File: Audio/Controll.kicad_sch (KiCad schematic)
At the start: 44 parts, among them J12 AMP1_PWR, J13 ROTARY_SW, J14 AMP_PWR_IN, J15 PD_IN, J16 AUDIO_IN, J17 OLED_PIN, J18 AMP1_LR, J19 AMP2_PWR, J20 AMP2_LR, J21 AMP3_PWR, J22 AMP4_PWR, J23 AMP5_PWR, J24 AMP3_LR, J25 AMP4_LR, J26 AMP5_LR, K1 AZ850P2-x, K10 AZ850P2-x, K2 AZ850P2-x, K3 AZ850P2-x, K4 AZ850P2-x, K5 AZ850P2-x, K6 AZ850P2-x, K7 AZ850P2-x, K8 AZ850P2-x, K9 AZ850P2-x, U5 BP5293-50, U6 ULN2803A, U7 ULN2803A, U8 ULN2803A

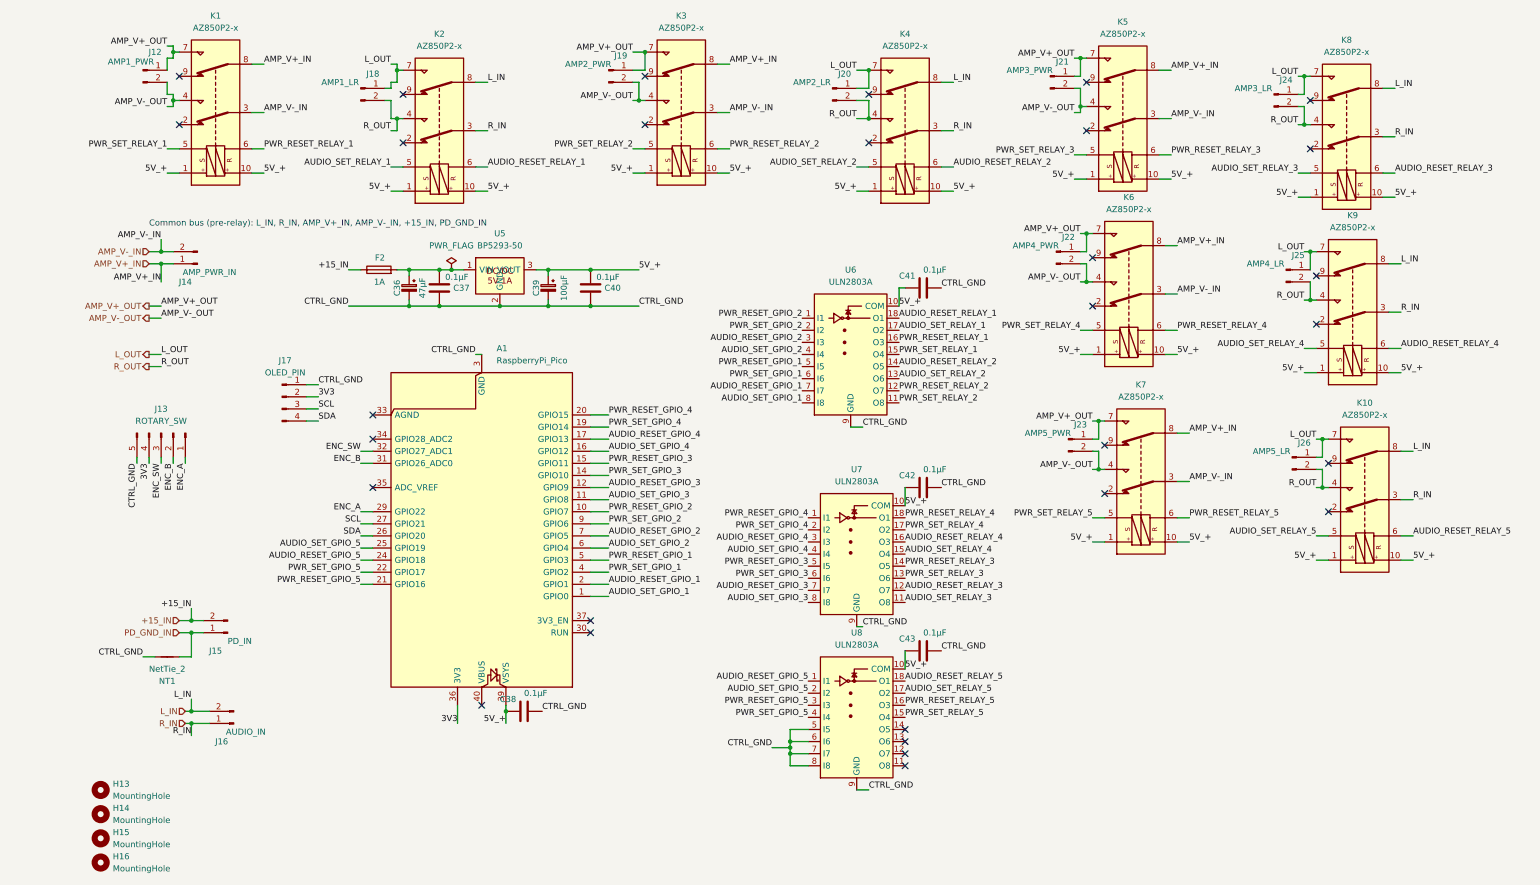
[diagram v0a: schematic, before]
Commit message: AudioCaseのリレー・EQネット整理と分割Gerberを再生成する。
Controllでアンプ別リレーネットを分離し、EQのバッファ入力をL/R_BUFF_INに改名。4枚分割PCBと発注用Gerberを更新し、RVパネルKiKit矩形とmacOS向けツール探索も修正。

Co-authored-by: Cursor <cursoragent@cursor.com>
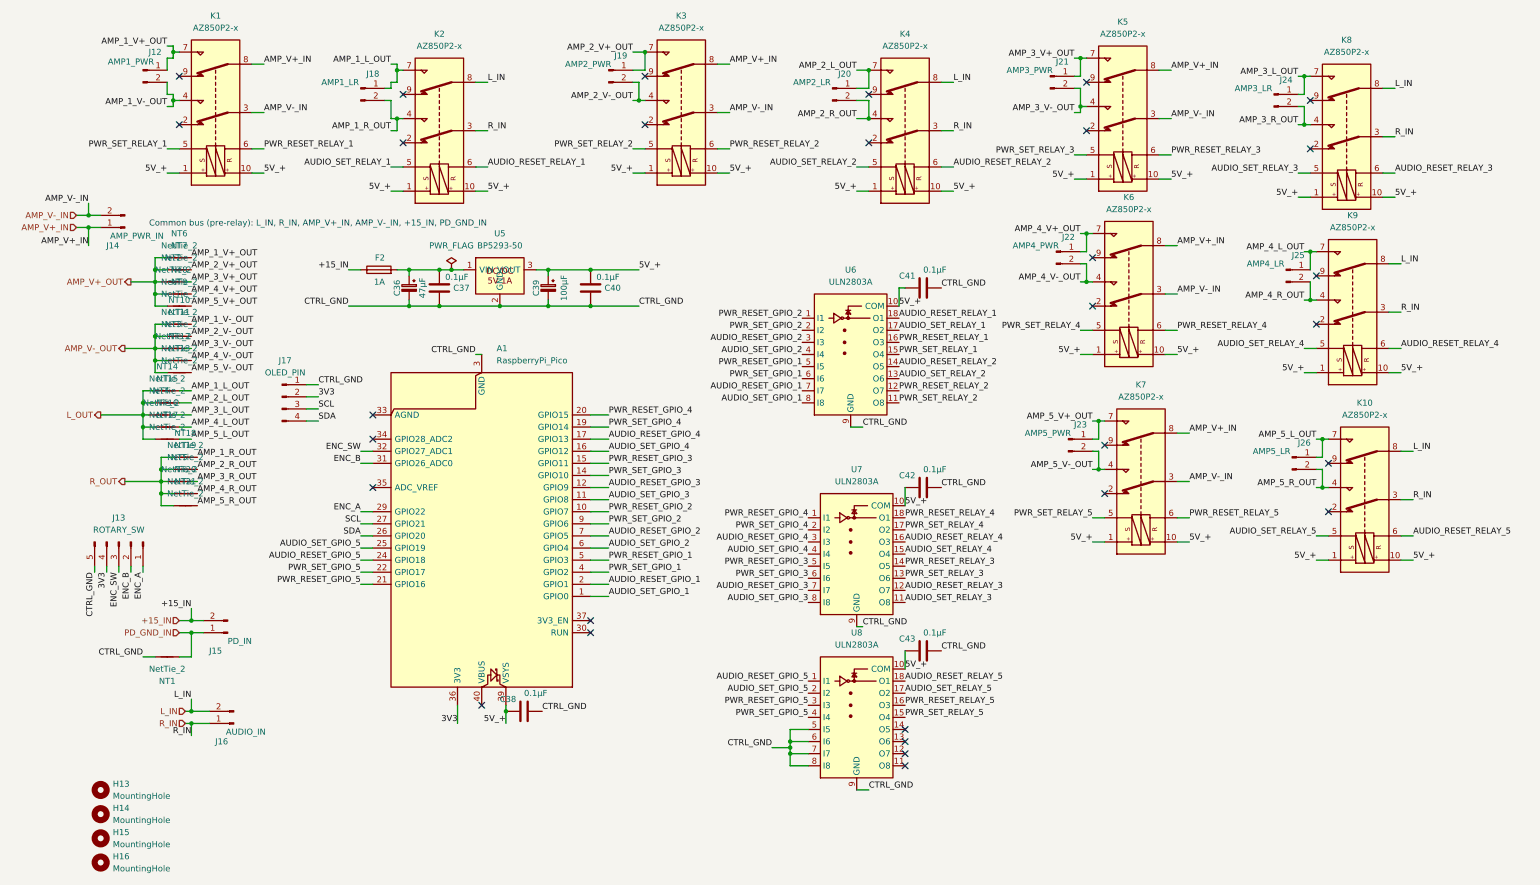
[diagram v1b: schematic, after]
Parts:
- added NT10, NT11, NT12, NT13, NT14, NT15, NT16, NT17, NT18, NT19, NT2, NT20, NT21, NT3, NT4, NT5, NT6, NT7, NT8, NT9: NetTie_2, symbol Device:NetTie_2
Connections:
- net AMP_V+_OUT: now also NT2.1, NT6.1, NT7.1, NT8.1, NT9.1; no longer J12.1 (Pin_1), J19.1 (Pin_1), J21.1 (Pin_1), J22.1 (Pin_1), J23.1 (Pin_1), K1.7, K3.7, K5.7, K6.7, K7.7
- net AMP_V-_OUT: now also NT10.1, NT11.1, NT12.1, NT13.1, NT3.1; no longer J12.2 (Pin_2), J19.2 (Pin_2), J21.2 (Pin_2), J22.2 (Pin_2), J23.2 (Pin_2), K1.4, K3.4, K5.4, K6.4, K7.4
- net L_OUT: now also NT14.1, NT15.1, NT16.1, NT17.1, NT4.1; no longer J18.1 (Pin_1), J20.1 (Pin_1), J24.1 (Pin_1), J25.1 (Pin_1), J26.1 (Pin_1), K10.7, K2.7, K4.7, K8.7, K9.7
- net R_OUT: now also NT18.1, NT19.1, NT20.1, NT21.1, NT5.1; no longer J18.2 (Pin_2), J20.2 (Pin_2), J24.2 (Pin_2), J25.2 (Pin_2), J26.2 (Pin_2), K10.4, K2.4, K4.4, K8.4, K9.4
- new net AMP_1_L_OUT: J18.1 (Pin_1), K2.7, NT14.2
- new net AMP_1_R_OUT: J18.2 (Pin_2), K2.4, NT18.2
- new net AMP_1_V+_OUT: J12.1 (Pin_1), K1.7, NT6.2
- new net AMP_1_V-_OUT: J12.2 (Pin_2), K1.4, NT10.2
- new net AMP_2_L_OUT: J20.1 (Pin_1), K4.7, NT15.2
- new net AMP_2_R_OUT: J20.2 (Pin_2), K4.4, NT19.2
- new net AMP_2_V+_OUT: J19.1 (Pin_1), K3.7, NT7.2
- new net AMP_2_V-_OUT: J19.2 (Pin_2), K3.4, NT11.2
- new net AMP_3_L_OUT: J24.1 (Pin_1), K8.7, NT4.2
- new net AMP_3_R_OUT: J24.2 (Pin_2), K8.4, NT5.2
- new net AMP_3_V+_OUT: J21.1 (Pin_1), K5.7, NT2.2
- new net AMP_3_V-_OUT: J21.2 (Pin_2), K5.4, NT3.2
- new net AMP_4_L_OUT: J25.1 (Pin_1), K9.7, NT16.2
- new net AMP_4_R_OUT: J25.2 (Pin_2), K9.4, NT20.2
- new net AMP_4_V+_OUT: J22.1 (Pin_1), K6.7, NT8.2
- new net AMP_4_V-_OUT: J22.2 (Pin_2), K6.4, NT12.2
- new net AMP_5_L_OUT: J26.1 (Pin_1), K10.7, NT17.2
- new net AMP_5_R_OUT: J26.2 (Pin_2), K10.4, NT21.2
- new net AMP_5_V+_OUT: J23.1 (Pin_1), K7.7, NT9.2
- new net AMP_5_V-_OUT: J23.2 (Pin_2), K7.4, NT13.2
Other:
- moved on the sheet: J13, J14

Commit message: MeasurementADC階層を追加し、基準計測用の電源・シンボルと進捗メモを整える。
KiCad 10向けにADC1804モジュール回路を移植し、親シート接続・Extrasライブラリ・ASFLフットプリント・ERCスナップショットを含める。

Co-authored-by: Cursor <cursoragent@cursor.com>
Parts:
- U5: footprint BP5293_ROHM:BP5293-50_ROHM_SIP-3 -> Library:BP5293-50_ROHM_SIP-3
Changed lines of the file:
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@@
 			)
 		)
-		(property "Footprint" "BP5293_ROHM:BP5293-50_ROHM_SIP-3"
+		(property "Footprint" "Library:BP5293-50_ROHM_SIP-3"
 			(at 101.6 76.2 0)
 			(hide yes)

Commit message: ヘッドホン出力と切替を追加し、S式検査をコミット前に走らせる。
Amp 後段を PHONE/MUTE/LINE に分け、NJM4556A の電流バッファとパッド付きボリュームを載せる。括弧崩れで回路図が開けなくなるのを check_sexpr と pre-commit で止める。

Co-authored-by: Cursor <cursoragent@cursor.com>
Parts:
- renumbered A1 to A501, C36 to C501, C37 to C502, C39 to C503, C40 to C504, C41 to C505, C42 to C506, C43 to C507, C38 to C508, F2 to F501, H13 to H501, H14 to H502, H15 to H503, H16 to H504, J12 to J501, J19 to J502, J21 to J503, J18 to J504, J20 to J505, J24 to J506, J14 to J507, J22 to J508, J25 to J509, J17 to J510, J23 to J511, J26 to J512, J13 to J513, J15 to J514, J16 to J515, K1 to K501, K3 to K502, K5 to K503, K2 to K504, K4 to K505, K8 to K506, K6 to K507, K9 to K508, K7 to K509, K10 to K510, NT6 to NT501, NT7 to NT502, NT2 to NT503, NT8 to NT504, NT9 to NT505, NT10 to NT506, NT11 to NT507, NT3 to NT508, NT12 to NT509, NT13 to NT510, NT14 to NT511, NT15 to NT512, NT4 to NT513, NT16 to NT514, NT17 to NT515, NT18 to NT516, NT19 to NT517, NT5 to NT518, NT20 to NT519, NT21 to NT520, NT1 to NT521, U5 to U501, U6 to U502, U7 to U503, U8 to U504
